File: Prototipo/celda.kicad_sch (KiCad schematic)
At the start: 15 parts, among them Q1 MMBT2222A, Q3 MMBT2907A, Q4 MMBT2222A

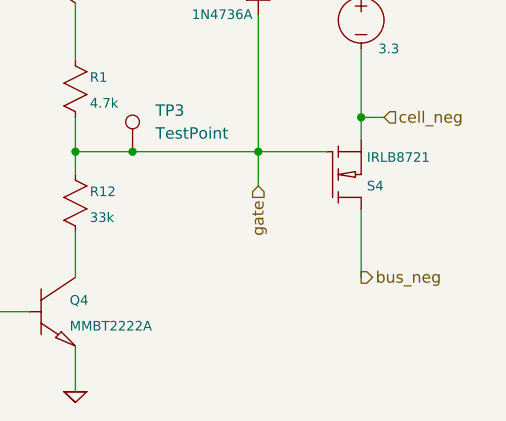
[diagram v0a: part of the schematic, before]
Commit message: Aplicar gitignore y dejar de trackear archivos innecesarios
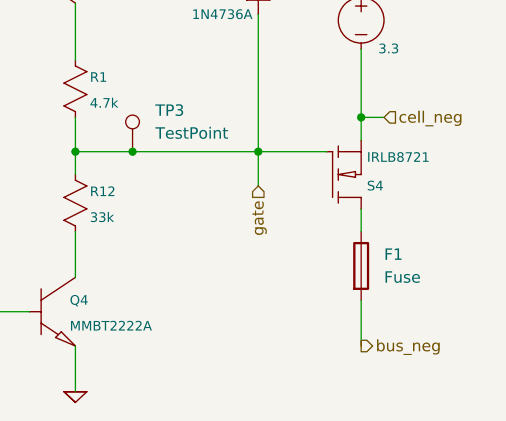
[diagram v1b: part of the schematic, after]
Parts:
- added F1: Fuse, Fuse:Fuseholder_Cylinder-5x20mm_Schurter_0031_8201_Horizontal_Open, symbol Device:Fuse
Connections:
- net bus_neg: now also F1.2; no longer S4.2 (D)
- new net: F1.1, S4.2 (D)
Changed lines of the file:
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@@
+	(wire
+		(pts
+			(xy 168.91 97.79) (xy 168.91 102.87)
+		)
+		(stroke
+			(width 0)
+			(type default)
+		)
+	)
 	(wire
 		(pts
@@
 	(wire
 		(pts
-			(xy 168.91 87.63) (xy 168.91 95.25)
+			(xy 168.91 87.63) (xy 168.91 90.17)
 		)
 		(stroke
@@
 	(hierarchical_label "bus_neg"
 		(shape output)
-		(at 168.91 95.25 0)
+		(at 168.91 102.87 0)
 		(effects
 			(font
@@
 					(unit 1)
 				)
+			)
+		)
+	)
+	(symbol
+		(lib_id "Device:Fuse")
+		(at 168.91 93.98 0)
+		(unit 1)
+		(exclude_from_sim no)
+		(in_bom yes)
+		(on_board yes)
+		(dnp no)
+		(property "Reference" "F1"
+			(at 171.45 92.7099 0)
+			(effects
+				(font
+					(size 1.27 1.27)
+				)
+				(justify left)
+			)
+		)
+		(property "Value" "Fuse"
+			(at 171.45 95.2499 0)
+			(effects
+				(font
+					(size 1.27 1.27)
+				)
+				(justify left)
+			)
+		)
+		(property "Footprint" "Fuse:Fuseholder_Cylinder-5x20mm_Schurter_0031_8201_Horizontal_Open"
+			(at 167.132 93.98 90)
+			(effects
+				(font
+					(size 1.27 1.27)
+				)
+				(hide yes)
+			)
+		)
+		(property "Datasheet" "~"
+			(at 168.91 93.98 0)
+			(effects
+				(font
+					(size 1.27 1.27)
+				)
+				(hide yes)
+			)
+		)
+		(property "Description" "Fuse"
+			(at 168.91 93.98 0)
+			(effects
+				(font
+					(size 1.27 1.27)
+				)
+				(hide yes)
+			)
+		)
+		(pin "1"
+		)
+		(pin "2"
+		)
+		(instances
+			(project ""
+				(path "/c9225433-a7fd-41e8-8162-e91e829dcb79/03228313-f124-4812-b57c-f34d519eb313"
+					(reference "F6")
+					(unit 1)
+				)
+				(path "/c9225433-a7fd-41e8-8162-e91e829dcb79/0b5b073f-7c77-4f5b-9d0c-04c95b3a5273"
+					(reference "F3")
+					(unit 1)
+				)
+				(path "/c9225433-a7fd-41e8-8162-e91e829dcb79/4139afdb-b33a-4b58-a58b-6904e64f0f54"
+					(reference "F2")
+					(unit 1)
+				)
+				(path "/c9225433-a7fd-41e8-8162-e91e829dcb79/5ccf80ef-8373-465f-9987-9fe1b9c88503"
+					(reference "F4")
+					(unit 1)
+				)
+				(path "/c9225433-a7fd-41e8-8162-e91e829dcb79/6883bdf6-06e3-408b-a2b6-79a0e0cc9199"
+					(reference "F1")
+					(unit 1)
+				)
+				(path "/c9225433-a7fd-41e8-8162-e91e829dcb79/9ecd509f-c28f-4327-a2e2-935fccd51d54"
+					(reference "F5")
+					(unit 1)
+				)

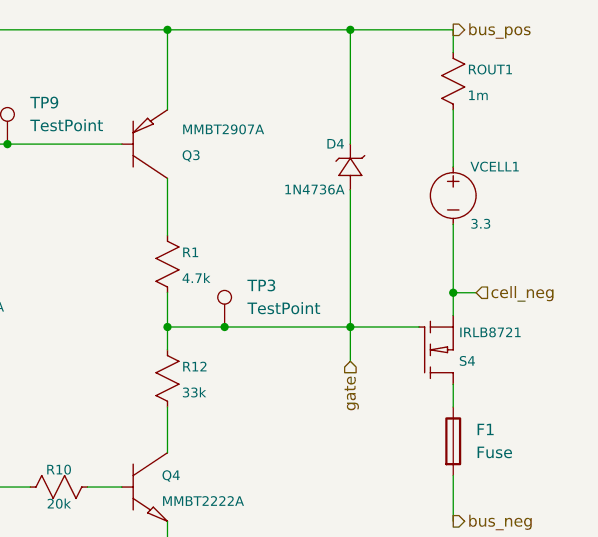
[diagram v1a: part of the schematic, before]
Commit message: Cambios de prototipo con el nuevo pmos
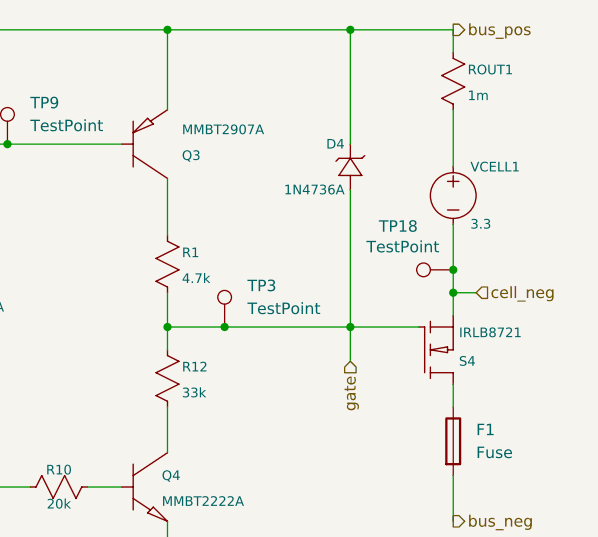
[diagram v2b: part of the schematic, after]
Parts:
- added TP18: TestPoint, TestPoint:TestPoint_Bridge_Pitch2.54mm_Drill1.0mm, symbol Connector:TestPoint
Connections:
- net cell_neg: now also TP18.1
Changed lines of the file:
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@@
+	)
+	(junction
+		(at 168.91 74.93)
+		(diameter 0)
+		(color 0 0 0 0)
 	)
 	(junction
@@
 	(wire
 		(pts
-			(xy 168.91 77.47) (xy 168.91 69.85)
+			(xy 168.91 77.47) (xy 168.91 74.93)
 		)
 		(stroke
@@
 		(pts
 			(xy 137.16 48.26) (xy 110.49 48.26)
+		)
+		(stroke
+			(width 0.1524)
+			(type solid)
+		)
+	)
+	(wire
+		(pts
+			(xy 168.91 74.93) (xy 168.91 69.85)
 		)
 		(stroke
@@
 					(unit 1)
 				)
+			)
+		)
+	)
+	(symbol
+		(lib_id "Connector:TestPoint")
+		(at 168.91 74.93 90)
+		(unit 1)
+		(exclude_from_sim no)
+		(in_bom yes)
+		(on_board yes)
+		(dnp no)
+		(property "Reference" "TP18"
+			(at 162.814 70.104 90)
+			(effects
+				(font
+					(size 1.27 1.27)
+				)
+			)
+		)
+		(property "Value" "TestPoint"
+			(at 163.322 72.39 90)
+			(effects
+				(font
+					(size 1.27 1.27)
+				)
+			)
+		)
+		(property "Footprint" "TestPoint:TestPoint_Bridge_Pitch2.54mm_Drill1.0mm"
+			(at 168.91 69.85 0)
+			(effects
+				(font
+					(size 1.27 1.27)
+				)
+				(hide yes)
+			)
+		)
+		(property "Datasheet" "~"
+			(at 168.91 69.85 0)
+			(effects
+				(font
+					(size 1.27 1.27)
+				)
+				(hide yes)
+			)
+		)
+		(property "Description" "test point"
+			(at 168.91 74.93 0)
+			(effects
+				(font
+					(size 1.27 1.27)
+				)
+				(hide yes)
+			)
+		)
+		(pin "1"
+		)
+		(instances
+			(project "prototipo"
+				(path "/c9225433-a7fd-41e8-8162-e91e829dcb79/03228313-f124-4812-b57c-f34d519eb313"
+					(reference "TP23")
+					(unit 1)
+				)
+				(path "/c9225433-a7fd-41e8-8162-e91e829dcb79/0b5b073f-7c77-4f5b-9d0c-04c95b3a5273"
+					(reference "TP20")
+					(unit 1)
+				)
+				(path "/c9225433-a7fd-41e8-8162-e91e829dcb79/4139afdb-b33a-4b58-a58b-6904e64f0f54"
+					(reference "TP19")
+					(unit 1)
+				)
+				(path "/c9225433-a7fd-41e8-8162-e91e829dcb79/5ccf80ef-8373-465f-9987-9fe1b9c88503"
+					(reference "TP21")
+					(unit 1)
+				)
+				(path "/c9225433-a7fd-41e8-8162-e91e829dcb79/6883bdf6-06e3-408b-a2b6-79a0e0cc9199"
+					(reference "TP18")
+					(unit 1)
+				)
+				(path "/c9225433-a7fd-41e8-8162-e91e829dcb79/9ecd509f-c28f-4327-a2e2-935fccd51d54"
+					(reference "TP22")
+					(unit 1)
+				)

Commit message: ruteo de un banco
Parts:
- VCELL1: footprint Battery:BatteryHolder_MPD_BK-18650-PC2 -> Huellas:BatteryHolder_MPD_BK-18650-PC2
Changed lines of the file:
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@@
 			)
 		)
-		(property "Footprint" "Battery:BatteryHolder_MPD_BK-18650-PC2"
+		(property "Footprint" "Huellas:BatteryHolder_MPD_BK-18650-PC2"
 			(at 168.91 62.23 0)
 			(effects

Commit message: cambio el zener y subo la listita de compras
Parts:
- F1: footprint Fuse:Fuseholder_Cylinder-5x20mm_Schurter_0031_8201_Horizontal_Open -> Huellas:Fuseholder_Cylinder-5x20mm_Schurter_0031_8201_Horizontal_Open
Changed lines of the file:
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@@
 			)
 		)
-		(property "Sim.Params" "R=${VALUE}"
+		(property "Sim.Params" "R=20k"
 			(at 104.14 76.2 0)
 			(effects
@@
 			)
 		)
-		(property "Sim.Params" "R=${VALUE}"
+		(property "Sim.Params" "R=1Meg"
 			(at 109.22 62.23 0)
 			(effects
@@
 			)
 		)
-		(property "Footprint" "Fuse:Fuseholder_Cylinder-5x20mm_Schurter_0031_8201_Horizontal_Open"
+		(property "Footprint" "Huellas:Fuseholder_Cylinder-5x20mm_Schurter_0031_8201_Horizontal_Open"
 			(at 167.132 93.98 90)
 			(effects
@@
 			)
 		)
-		(property "Sim.Params" "R=${VALUE}"
+		(property "Sim.Params" "R=4.7k"
 			(at 135.89 69.85 0)
 			(effects
@@
 			)
 		)
-		(property "Sim.Params" "type=\"V\" model=\"${VALUE}\" "
+		(property "Sim.Params" "type=\"V\" model=\"3.3\" "
 			(at 168.91 62.23 0)
 			(effects
@@
 			)
 		)
-		(property "Sim.Params" "R=${VALUE}"
+		(property "Sim.Params" "R=1m"
 			(at 167.64 49.53 0)
 			(effects
@@
 			)
 		)
-		(property "Sim.Params" "R=${VALUE}"
+		(property "Sim.Params" "R=20k"
 			(at 129.54 97.79 0)
 			(effects
@@
 			)
 		)
-		(property "Sim.Params" "R=${VALUE}"
+		(property "Sim.Params" "R=33k"
 			(at 135.89 82.55 0)
 			(effects
@@
 			)
 		)
-		(property "Sim.Params" "R=${VALUE}"
+		(property "Sim.Params" "R=10Meg"
 			(at 109.22 50.8 0)
 			(effects

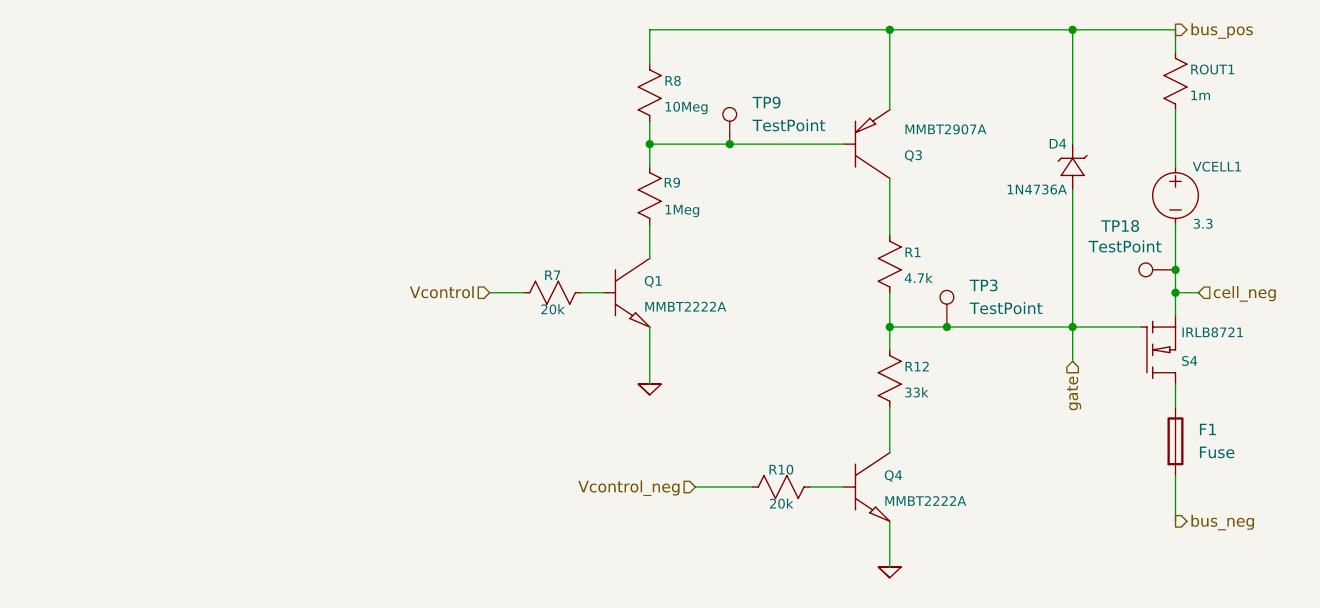
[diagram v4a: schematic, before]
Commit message: termino de reacomodar las celdas con la disposición nueva, faltan las conexiones de la entrada.
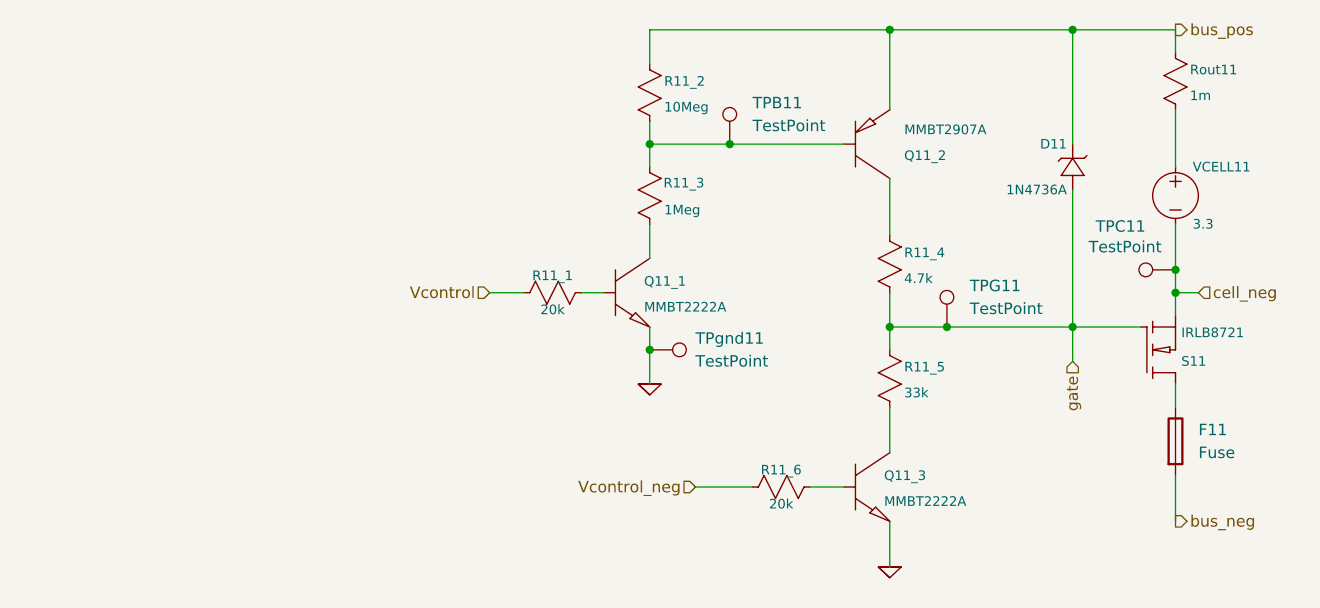
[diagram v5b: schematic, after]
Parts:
- added TPgnd11: TestPoint, TestPoint:TestPoint_Bridge_Pitch2.54mm_Drill1.0mm, symbol Connector:TestPoint
- renumbered D4 to D11, F1 to F11, Q1 to Q11_1, Q3 to Q11_2, Q4 to Q11_3, R7 to R11_1, R8 to R11_2, R9 to R11_3, R1 to R11_4, R12 to R11_5, R10 to R11_6, ROUT1 to Rout11, S4 to S11, TP9 to TPB11, TP18 to TPC11, TP3 to TPG11, VCELL1 to VCELL11
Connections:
- net 0: now also TPgnd11.1

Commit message: Propuesta de conexión de las entradas
no me gusta la opción, pero esta conectado
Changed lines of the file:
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@@
 	)
 	(symbol
-		(lib_id "ltspice:GND")
+		(lib_id "power:GND")
 		(at 137.16 107.95 0)
 		(unit 1)
@@
 			)
 		)
-		(property "Description" ""
+		(property "Description" "Power symbol creates a global label with name \"GND\" , ground"
 			(at 137.16 107.95 0)
 			(effects
@@
 			)
 		)
-		(pin ""
+		(pin "1"
 		)
 		(instances
@@
 	)
 	(symbol
-		(lib_id "ltspice:GND")
+		(lib_id "power:GND")
 		(at 110.49 87.63 0)
 		(unit 1)
@@
 			)
 		)
-		(property "Description" ""
+		(property "Description" "Power symbol creates a global label with name \"GND\" , ground"
 			(at 110.49 87.63 0)
 			(effects
@@
 			)
 		)
-		(pin ""
+		(pin "1"
 		)
 		(instances

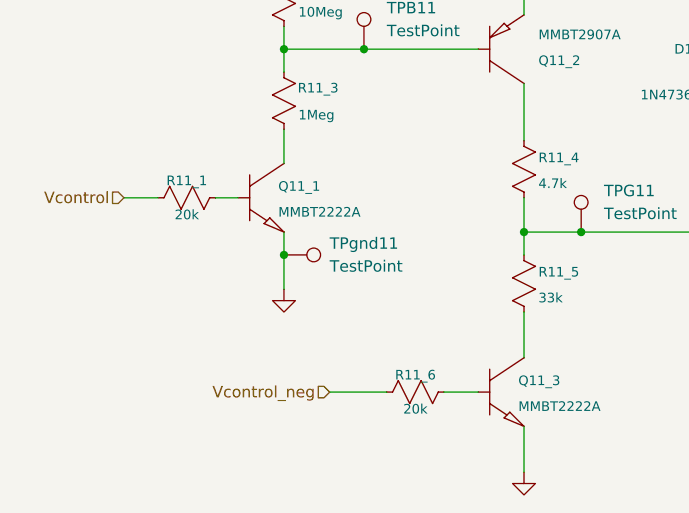
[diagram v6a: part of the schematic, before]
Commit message: conexión interna de celdas inferiores
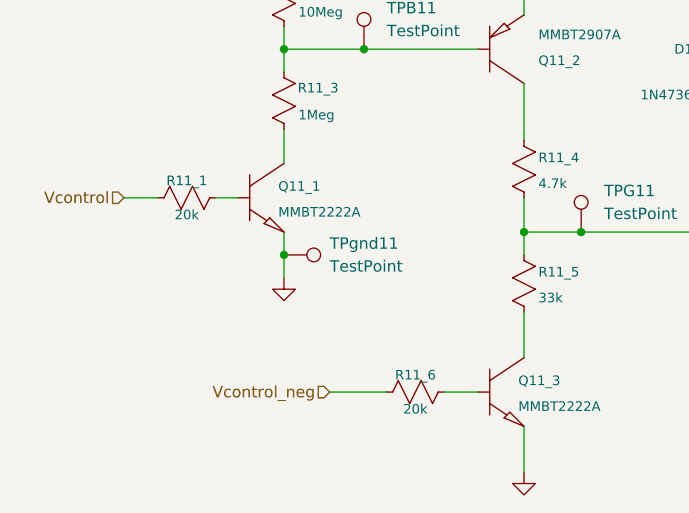
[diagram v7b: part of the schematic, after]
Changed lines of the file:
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@@
 	(wire
 		(pts
-			(xy 110.49 87.63) (xy 110.49 83.82)
+			(xy 110.49 86.36) (xy 110.49 83.82)
 		)
 		(stroke
@@
 	(symbol
 		(lib_id "power:GND")
-		(at 110.49 87.63 0)
+		(at 110.49 86.36 0)
 		(unit 1)
 		(exclude_from_sim no)
@@
 		(dnp no)
 		(property "Reference" "#GND08"
-			(at 110.49 87.63 0)
+			(at 110.49 86.36 0)
 			(effects
 				(font
@@
 		)
 		(property "Value" "0"
-			(at 110.49 87.63 0)
+			(at 110.49 86.36 0)
 			(effects
 				(font
@@
 		)
 		(property "Footprint" ""
-			(at 110.49 87.63 0)
+			(at 110.49 86.36 0)
 			(effects
 				(font
@@
 		)
 		(property "Datasheet" ""
-			(at 110.49 87.63 0)
+			(at 110.49 86.36 0)
 			(effects
 				(font
@@
 		)
 		(property "Description" "Power symbol creates a global label with name \"GND\" , ground"
-			(at 110.49 87.63 0)
-			(effects
-				(font
+			(at 110.49 86.36 0)
+			(effects
+				(font

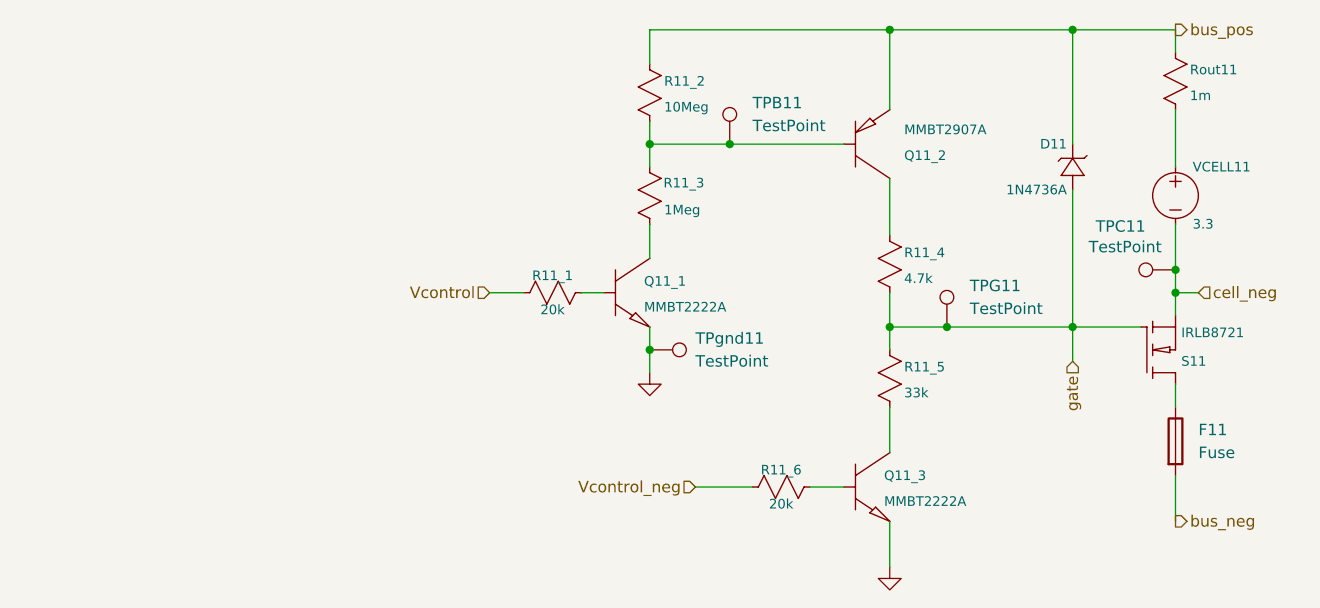
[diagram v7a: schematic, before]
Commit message: Suma leds a kicad, falta rutear
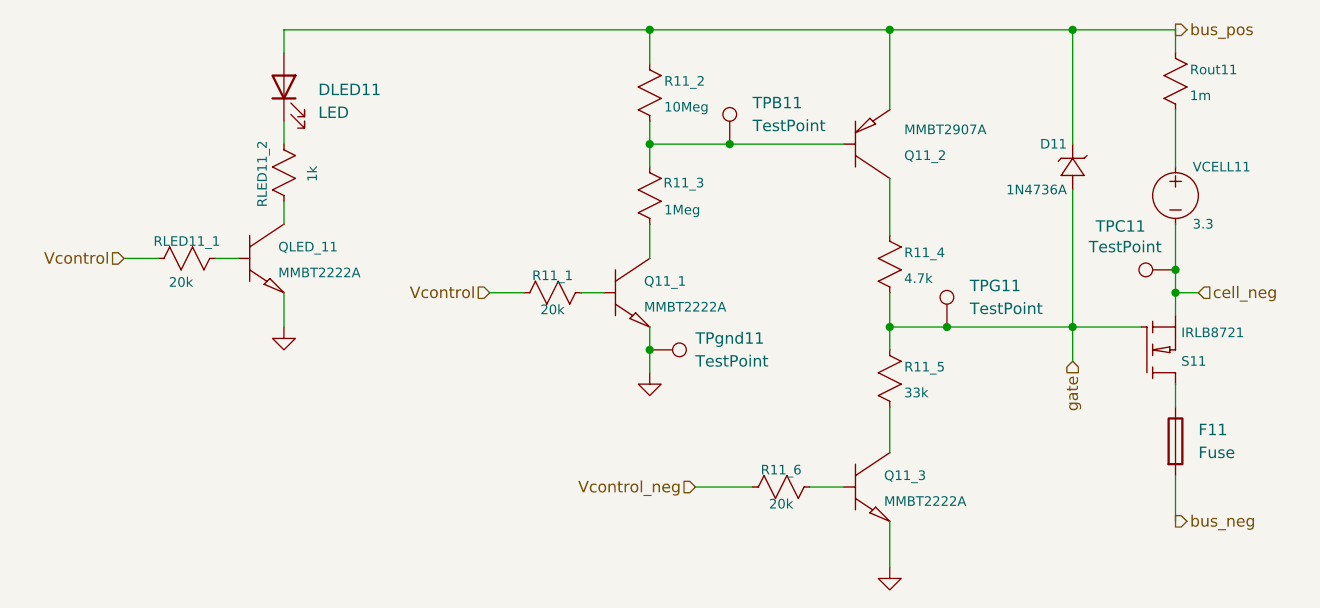
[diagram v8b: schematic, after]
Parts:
- added DLED11: LED, LED_THT:LED_D5.0mm, symbol Device:LED
- added QLED_11: MMBT2222A, Package_TO_SOT_SMD:SOT-23-3, symbol modificados:npn
- added RLED11_1: 20k, Resistor_THT:R_Axial_DIN0207_L6.3mm_D2.5mm_P7.62mm_Horizontal, symbol ltspice:res
- added RLED11_2: 1k, Resistor_THT:R_Axial_DIN0207_L6.3mm_D2.5mm_P7.62mm_Horizontal, symbol ltspice:res
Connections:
- net 0: now also QLED_11.2 (E)
- net Vcontrol: now also RLED11_1.2
- net bus_pos: now also DLED11.2 (A)
- new net: QLED_11.1 (B), RLED11_1.1
- new net: DLED11.1 (K), RLED11_2.1
- new net: QLED_11.3 (C), RLED11_2.2
